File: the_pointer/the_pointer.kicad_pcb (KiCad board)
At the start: 4 copper layers, 24 x 75 mm, 110 parts, among them J1 Screw_Terminal_01x06, J2 Conn_Coaxial, J3 BMI-S-209-F, J4 Screw_Terminal_01x06, J5 R41-B583A, J6 BMI-S-209-F, Q1 AS2312, Q2 AS2312, Q3 AS2312, Q4 AS2312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

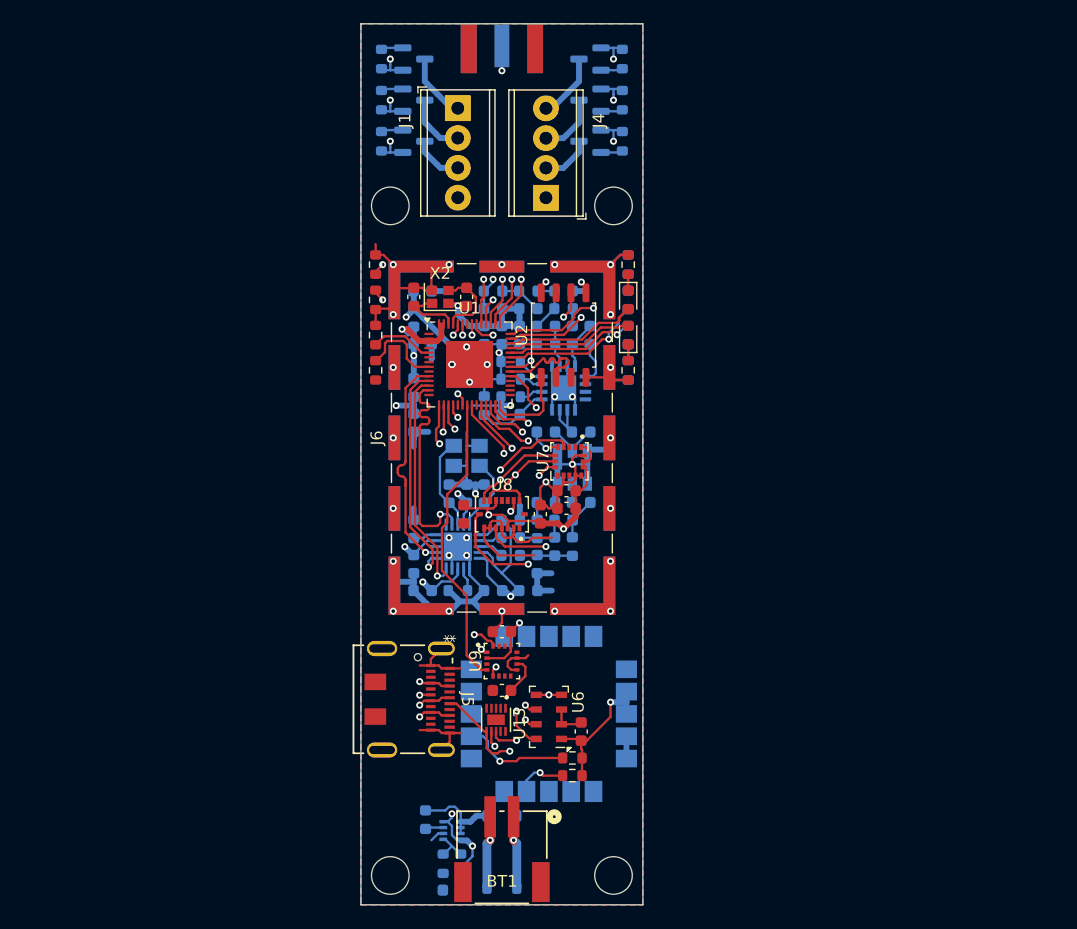
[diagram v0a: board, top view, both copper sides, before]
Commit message: Routed Pointer RF transmitter
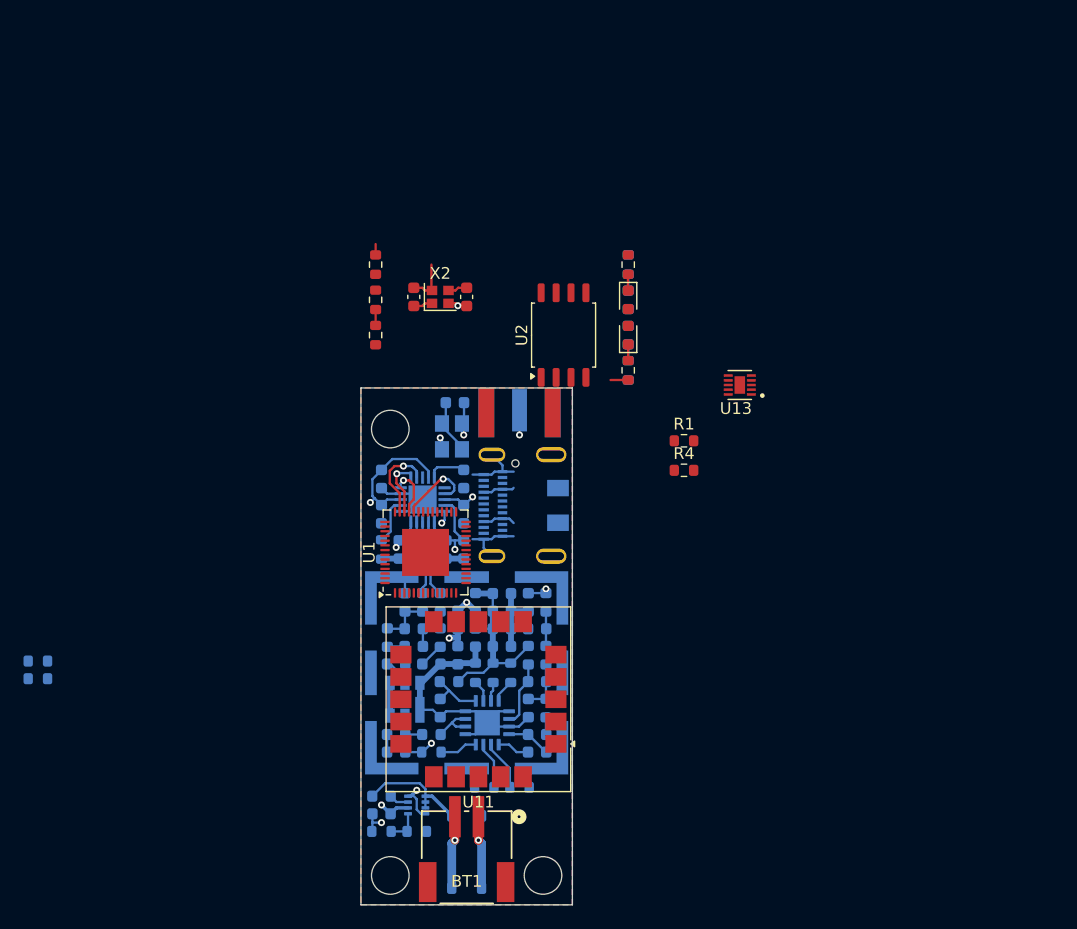
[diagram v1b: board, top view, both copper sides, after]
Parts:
- removed C10, C8: 10u, Capacitor_SMD:C_0603_1608Metric
- removed C11, C12: 100n, Capacitor_SMD:C_0603_1608Metric
- removed C6, C7: 0.1u, Capacitor_SMD:C_0603_1608Metric
- removed C9: 1u, Capacitor_SMD:C_0603_1608Metric
- removed H4: MountingHole, MountingHole:MountingHole_3.2mm_M3
- removed J1, J4: Screw_Terminal_01x06, TerminalBlock_Phoenix:TerminalBlock_Phoenix_MPT-0,5-4-2.54_1x04_P2.54mm_Horizontal
- removed J6: BMI-S-209-F, RF_Shielding:Laird_Technologies_BMI-S-209-F_29.36x18.50mm
- removed Q1, Q2, Q3, Q4, Q5, Q6: AS2312, Package_TO_SOT_SMD:SOT-23
- removed R11, R5, R6, R7, R8, R9: 10k, Resistor_SMD:R_0603_1608Metric
- removed U6: MS5607-02BA, Package_LGA:LGA-8_3x5mm_P1.25mm
- removed U7: H3LIS200DLTR, locals_but_working_PLEASE:H3LIS200DLTR
- removed U8: BMI088, locals_but_working_PLEASE:BMI088
- removed U9: MMC5883MA, locals_but_working_PLEASE:MMC5983MA
- added R1: 10k, Resistor_SMD:R_0603_1608Metric, F.Cu at (227.5, 60.5)
- added R61: 10k, Resistor_SMD:R_0603_1608Metric, B.Cu at (213.5, 90.0)
- added R71: 10k, Resistor_SMD:R_0603_1608Metric, B.Cu at (210.5, 90.0)
- added R81: 10k, Resistor_SMD:R_0603_1608Metric, B.Cu at (206.0, 87.0)
- J3: value BMI-S-209-F -> BMI-S-202-F; footprint RF_Shielding:Laird_Technologies_BMI-S-209-F_29.36x18.50mm -> RF_Shielding:Laird_Technologies_BMI-S-202-F_16.50x16.50mm
- J5, R18, R19: moved to B.Cu
- R4, U11: moved to F.Cu
- U1: value ESP32-S3FN8 -> ESP32-S2FH4
- moved R18 46.2 mm to (172.5, 80.8), turned to 0 degrees
- moved R19 46.2 mm to (172.5, 79.2), turned to 0 degrees
- moved R4 43.5 mm to (227.5, 63.0), turned to 0 degrees
- moved C52 35.8 mm to (215.0, 87.0), turned to 180 degrees
- moved C24 35.6 mm to (214.2, 83.2), turned to 90 degrees
- moved U13 35.3 mm to (232.2, 55.8), turned to 180 degrees
- moved C3 34.8 mm to (203.0, 87.0), turned to 0 degrees
- moved C22 34.1 mm to (215.0, 85.5), turned to 180 degrees
- moved L22 34.0 mm to (215.8, 83.2), turned to 90 degrees
- moved J2 31.0 mm to (213.5, 58.1)
- moved L23 31.0 mm to (215.8, 78.8), turned to -90 degrees
- moved C21 30.3 mm to (215.0, 81.0), turned to 180 degrees
- moved U4 29.2 mm to (210.8, 84.5), turned to 180 degrees
- moved C125 28.7 mm to (203.0, 85.5)
- moved L25 28.7 mm to (206.0, 85.5), turned to 0 degrees
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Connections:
- R12 pad 1: Net-(U1-GPIO46) -> Net-(U1-GPIO45)
- R13 pad 1: Net-(U1-GPIO45) -> Net-(U1-GPIO46)
- R4 pad 1: T_{1} -> VCC
- R4 pad 2: GND -> Net-(U13-~{ACK})
- U1 pad 1: unconnected-(U1-LNA_IN-Pad1) -> VCC
- U1 pad 10: SDO3 -> unconnected-(U1-GPIO5-Pad10)
- U1 pad 11: SCLK3 -> unconnected-(U1-GPIO6-Pad11)
- U1 pad 12: SDI3 -> unconnected-(U1-GPIO7-Pad12)
- U1 pad 13: ~{CS}_{RF} -> unconnected-(U1-GPIO8-Pad13)
- U1 pad 15: ~{CS}_{MAIN_ACC} -> unconnected-(U1-GPIO10-Pad15)
- U1 pad 16: SDI2 -> unconnected-(U1-GPIO11-Pad16)
- U1 pad 17: SCLK2 -> unconnected-(U1-GPIO12-Pad17)
- U1 pad 18: SDO2 -> unconnected-(U1-GPIO13-Pad18)
- U1 pad 2: VCC -> unconnected-(U1-LNA_IN-Pad2)
- U1 pad 21: ~{CS}_{MAG} -> unconnected-(U1-XTAL_32K_P-Pad21)
- U1 pad 22: ~{CS}_{GYRO} -> unconnected-(U1-XTAL_32K_N-Pad22)
- U1 pad 24: ~{CS}_{BARO} -> unconnected-(U1-DAC_2-Pad24)
- U1 pad 27: ~{CS}_{HI_ACC} -> VCC
- U1 pad 28: ~{CS}_{FLASH} -> unconnected-(U1-GPIO21-Pad28)
- U1 pad 30: unconnected-(U1-SPIHD-Pad30) -> VCC
- U1 pad 33: SCLK1 -> ~{CS}_{FLASH}
- U1 pad 34: SDO1 -> SCLK1
- U1 pad 35: SDI1 -> SDO1
- U1 pad 36: unconnected-(U1-SPICLK_N-Pad36) -> SDI1
- U1 pad 37: LED3 -> unconnected-(U1-GPIO33-Pad37)
- U1 pad 38: LED4 -> ~{CS}_{RF}
- U1 pad 39: LED2 -> SDI3
- U1 pad 4: unconnected-(U1-CHIP_PU-Pad4) -> VCC
- U1 pad 40: LED1 -> SCLK3
- U1 pad 41: SCL1 -> SDO3
- U1 pad 42: SDA1 -> unconnected-(U1-GPIO38-Pad42)
- U1 pad 43: T_{4} -> unconnected-(U1-MTCK-Pad43)
- U1 pad 44: T_{5} -> unconnected-(U1-MTD0-Pad44)
- U1 pad 45: T_{6} -> VCC
- U1 pad 46: VCC -> unconnected-(U1-MDTI-Pad46)
- U1 pad 47: T_{1} -> unconnected-(U1-MTMS-Pad47)
- U1 pad 48: T_{2} -> unconnected-(U1-U0TXD-Pad48)
- U1 pad 49: T_{3} -> unconnected-(U1-U0RXD-Pad49)
- U1 pad 50: unconnected-(U1-U0RXD-Pad50) -> Net-(U1-GPIO45)
- U1 pad 51: Net-(U1-GPIO45) -> VCC
- U1 pad 52: Net-(U1-GPIO46) -> XTAL_N
- U1 pad 53: XTAL_N -> XTAL_P
- U1 pad 54: XTAL_P -> VCC
- U1 pad 55: VCC -> Net-(U1-GPIO46)
- U1 pad 56: VCC -> unconnected-(U1-CHIP_PU-Pad56)
- U1 pad 8: Net-(U1-GPIO3) -> unconnected-(U1-GPIO3-Pad8)
- U13 pad 10: unconnected-(U13-VBUS_10-Pad10) -> VCC
- U13 pad 3: unconnected-(U13-~{EN}-Pad3) -> Net-(U13-~{EN})
- U13 pad 4: unconnected-(U13-~{ACK}-Pad4) -> Net-(U13-~{ACK})
- U13 pad 5: unconnected-(U13-ID-Pad5) -> USB_ID
- U13 pad 9: unconnected-(U13-VBUS_9-Pad9) -> VCC
- U4 pad 6: unconnected-(U4-HGM-Pad6) -> HGM
- U4 pad 7: unconnected-(U4-LNA-EN-Pad7) -> LNA_EN
- U4 pad 8: unconnected-(U4-PA-EN-Pad8) -> PA_EN
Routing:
- net GND: track 197.8 -> 77.7 mm, vias 38 -> 2
- net SCL1: track 62.8 -> 0.00 mm, vias 2 -> 0
- net USB_D-: track 62.2 -> 0.00 mm, vias 3 -> 0
- net SDA1: track 59.7 -> 0.00 mm, vias 2 -> 0
- net USB_D+: track 57.7 -> 0.00 mm, vias 3 -> 0
- net VCC: track 68.1 -> 15.7 mm, vias 13 -> 4
- net SCLK2: track 50.8 -> 0.00 mm, vias 5 -> 0
- net SDI2: track 45.9 -> 0.00 mm, vias 4 -> 0
- net SDO2: track 42.3 -> 0.00 mm, vias 4 -> 0
- net ~{CS}_{BARO}: track 30.1 -> 0.00 mm, vias 2 -> 0
- net T_{6}: track 29.7 -> 0.00 mm, vias 2 -> 0
- net T_{1}: track 28.7 -> 0.00 mm, vias 2 -> 0
- net T_{2}: track 28.5 -> 0.00 mm, vias 2 -> 0
- net T_{5}: track 26.0 -> 0.00 mm, vias 2 -> 0
- net ~{CS}_{MAG}: track 25.3 -> 0.00 mm
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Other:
- board size 24 x 75 mm -> 18 x 44 mm

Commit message: Routed Pointer GPS
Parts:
- R18, R19: moved to F.Cu
- moved R18 40.2 mm to (212.0, 73.5), turned to 180 degrees
- moved R13 30.2 mm to (201.2, 75.8), turned to -90 degrees
- moved R19 28.9 mm to (201.2, 81.8), turned to 90 degrees
- moved R10 27.2 mm to (201.2, 78.8), turned to -90 degrees
- moved C13 25.6 mm to (215.8, 71.2), turned to -90 degrees
- moved X2 24.0 mm to (213.5, 71.2), turned to 180 degrees
- moved D2 23.6 mm to (226.8, 71.8)
- moved D3 23.6 mm to (226.8, 74.8)
- moved R14 23.6 mm to (226.8, 68.8)
- moved R15 23.6 mm to (226.8, 77.8)
- moved C14 23.1 mm to (211.2, 71.2), turned to -90 degrees
- moved D4 23.0 mm to (231.0, 70.0)
- moved D5 23.0 mm to (231.0, 73.0)
- moved R16 23.0 mm to (231.0, 67.0)
- moved R17 23.0 mm to (231.0, 76.0)
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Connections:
- U1 pad 16: unconnected-(U1-GPIO11-Pad16) -> LED4
- U1 pad 17: unconnected-(U1-GPIO12-Pad17) -> LED3
- U1 pad 18: unconnected-(U1-GPIO13-Pad18) -> LED2
- U1 pad 19: unconnected-(U1-GPIO14-Pad19) -> LED1
- U1 pad 7: unconnected-(U1-GPIO2-Pad7) -> SCL1
- U1 pad 8: unconnected-(U1-GPIO3-Pad8) -> SDA1
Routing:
- net VCC: track 15.7 -> 46.5 mm, vias 4 -> 8
- net XTAL_P: track 1.64 -> 27.5 mm, vias 0 -> 2
- net XTAL_N: track 1.64 -> 27.4 mm, vias 0 -> 2
- net /Transmitter/RF_OUT: track 3.97 -> 20.5 mm
- net SDA1: track 0.00 -> 13.5 mm
- net SDI1: track 0.00 -> 11.8 mm
- net SCL1: track 0.00 -> 11.6 mm
- net SCLK1: track 0.00 -> 9.97 mm, vias 0 -> 2
- net USB_D+: track 0.00 -> 9.05 mm, vias 0 -> 1
- net USB_D-: track 0.00 -> 7.85 mm, vias 0 -> 1
- net VCC_{CC1101}: track 49.8 -> 55.9 mm, vias 4 -> 5
- net SDO1: track 0.00 -> 5.57 mm
- net XOSC_Q2: track 12.3 -> 17.8 mm
- net GND: track 77.7 -> 73.7 mm, vias 2 -> 4
- net ~{CS}_{FLASH}: track 0.00 -> 3.55 mm
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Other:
- board size 18 x 44 mm -> 18 x 46.5 mm

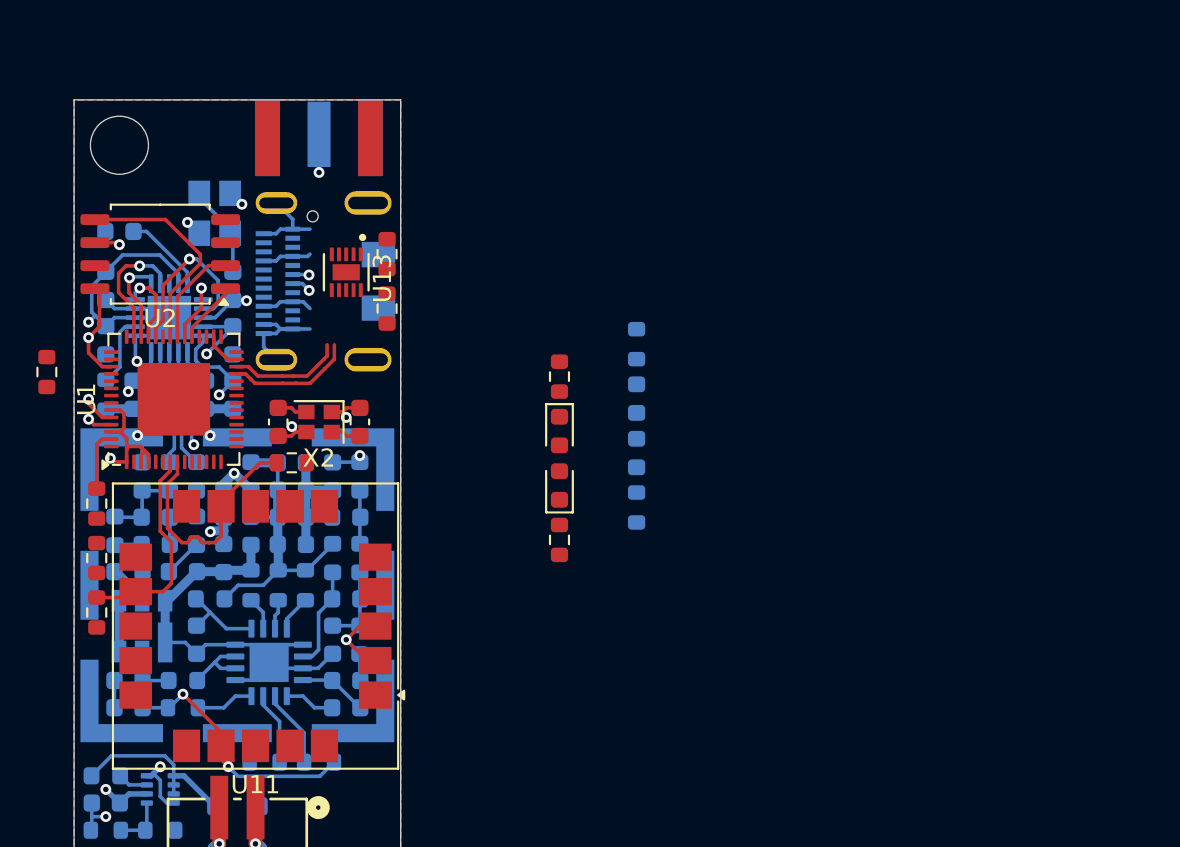
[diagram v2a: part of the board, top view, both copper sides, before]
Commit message: Swapped Pointer to ESP32-C3FH4
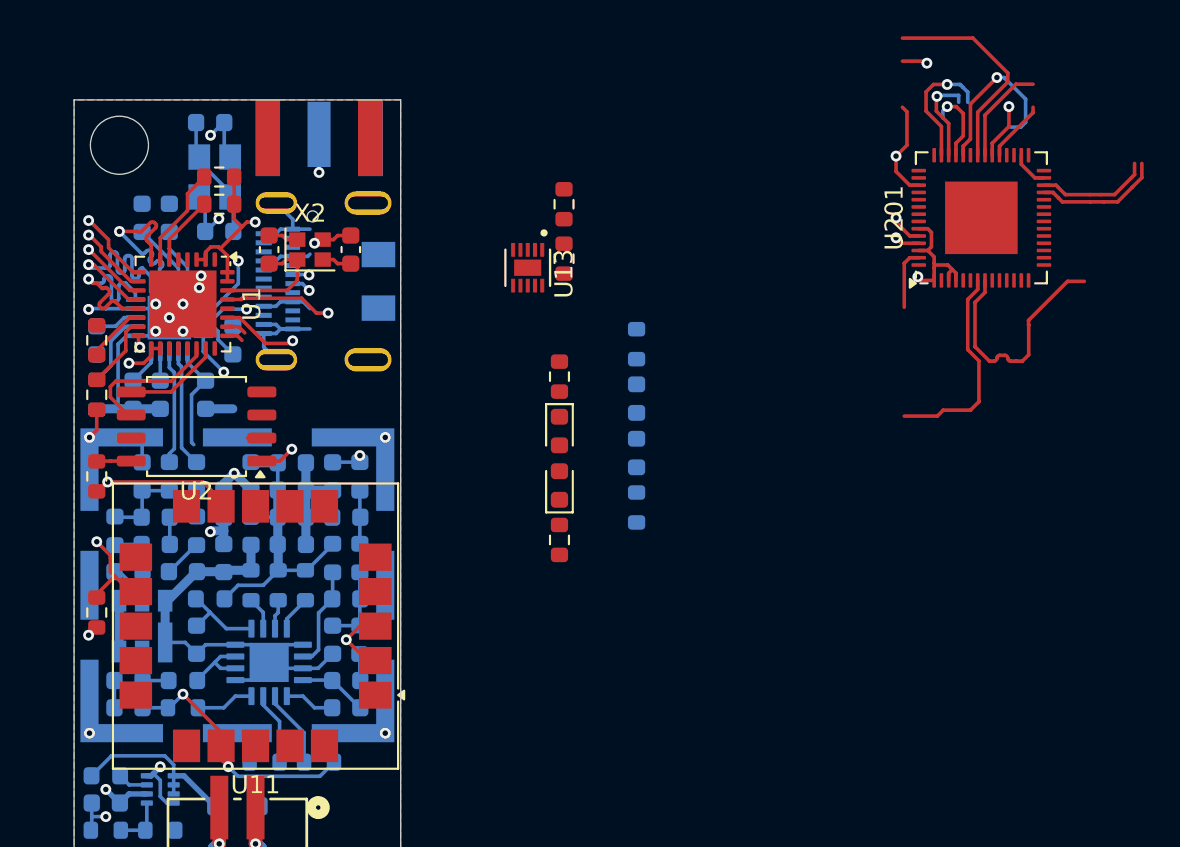
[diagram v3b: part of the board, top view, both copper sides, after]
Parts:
- added R5: 10k, Resistor_SMD:R_0603_1608Metric, F.Cu at (208.0, 57.8)
- added U1: ESP32-C3FH4, Package_DFN_QFN:QFN-32-1EP_5x5mm_P0.5mm_EP3.7x3.7mm, F.Cu at (206.0, 64.8)
- moved U201 45.6 mm to (250.0, 60.0)
- moved R10 20.6 mm to (208.0, 59.2), turned to 0 degrees
- moved R18 10.8 mm to (201.2, 74.2), turned to -90 degrees
- moved C13 10.7 mm to (210.8, 61.8), turned to 90 degrees
- moved C14 10.3 mm to (215.2, 61.8), turned to 90 degrees
- moved R1 10.1 mm to (227.0, 62.2)
- moved R4 10.1 mm to (227.0, 59.2)
- moved U13 10.0 mm to (225.0, 62.8)
- moved U2 9.71 mm to (206.8, 71.5)
- moved X2 9.51 mm to (213.0, 61.8), turned to 0 degrees
- moved C81 9.09 mm to (207.5, 54.8), turned to 180 degrees
- moved C101 9.03 mm to (208.0, 60.8), turned to 180 degrees
- moved R13 6.00 mm to (201.2, 69.8)
- moved C41 4.25 mm to (203.8, 60.0), turned to -90 degrees
- moved R12 3.26 mm to (201.2, 66.8)
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- renumbered U1 to U201
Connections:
- R10 pad 1: Net-(U1-GPIO0) -> Net-(U1-GPIO2)
- R10 pad 2: GND -> VCC
- R12 pad 1: Net-(U1-GPIO45) -> Net-(U1-GPIO8)
- R12 pad 2: GND -> VCC
- R13 pad 1: Net-(U1-GPIO46) -> Net-(U1-GPIO9)
- U201 pad 5: Net-(U1-GPIO0) -> unconnected-(U201-GPIO0-Pad5)
- U201 pad 50: Net-(U1-GPIO45) -> unconnected-(U201-GPIO45-Pad50)
- U201 pad 55: Net-(U1-GPIO46) -> unconnected-(U201-GPIO46-Pad55)
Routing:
- net VCC_{CC1101}: track 55.9 -> 21.8 mm, vias 5 -> 1
- net SCL1: track 11.6 -> 38.9 mm, vias 0 -> 2
- net SDA1: track 13.5 -> 40.4 mm, vias 0 -> 2
- net VCC: track 46.5 -> 65.0 mm, vias 8 -> 12
- net ~{CS}_{FLASH}: track 3.55 -> 19.0 mm, vias 0 -> 2
- net ~{CS}_{RF}: track 9.34 -> 22.1 mm, vias 1 -> 3
- net SCLK3: track 5.14 -> 16.9 mm, vias 1 -> 2
- net SDI3: track 4.23 -> 14.9 mm, vias 1 -> 2
- net SDO3: track 7.04 -> 16.6 mm, vias 1 -> 2
- net XTAL_N: track 27.4 -> 35.9 mm, vias 2 -> 3
- net SCLK1: track 9.97 -> 18.0 mm
- net GND: track 73.7 -> 80.9 mm, vias 4 -> 13
- net Net-(U1-CHIP_EN): track 0.00 -> 5.55 mm
- net SDI1: track 11.8 -> 17.2 mm
- net Net-(U1-GPIO9): track 0.00 -> 4.12 mm
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
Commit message: Continued routing Pointer
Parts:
- removed U201: ESP32-S2FH4, Package_DFN_QFN:QFN-56-1EP_7x7mm_P0.4mm_EP4x4mm
- moved R1 14.9 mm to (216.0, 72.2), turned to 180 degrees
- moved R4 14.9 mm to (216.8, 70.0)
- moved U13 13.1 mm to (214.2, 70.2), turned to 180 degrees
- moved C181 1.50 mm to (201.2, 65.2), turned to -90 degrees
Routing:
- net XTAL_N: track 35.9 -> 10.5 mm, vias 3 -> 2
- net XTAL_P: track 29.8 -> 6.87 mm, vias 1 -> 0
- net SDA1: track 40.4 -> 26.9 mm
- net SDI1: track 17.2 -> 5.37 mm
- net SCL1: track 38.9 -> 27.3 mm
- net ~{CS}_{RF}: track 22.1 -> 11.0 mm, vias 3 -> 2
- net SCLK1: track 18.0 -> 8.00 mm, vias 2 -> 0
- net GND: track 80.9 -> 89.7 mm
- net SDO3: track 16.6 -> 9.57 mm, vias 2 -> 1
- net VCC: track 65.0 -> 58.1 mm, vias 12 -> 11
- net USB_D-: track 8.76 -> 14.0 mm
- net SCLK3: track 16.9 -> 11.8 mm, vias 2 -> 1
- net SDI3: track 14.9 -> 10.7 mm, vias 2 -> 1
- net USB_D+: track 10.2 -> 14.2 mm, vias 1 -> 2
- net unconnected-(U201-GPIO46-Pad55): track 3.35 -> 0.00 mm
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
